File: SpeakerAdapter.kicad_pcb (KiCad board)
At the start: 2 copper layers, 14 x 12 mm, 2 parts, among them J1 Terminal Block, J2 JST-PH

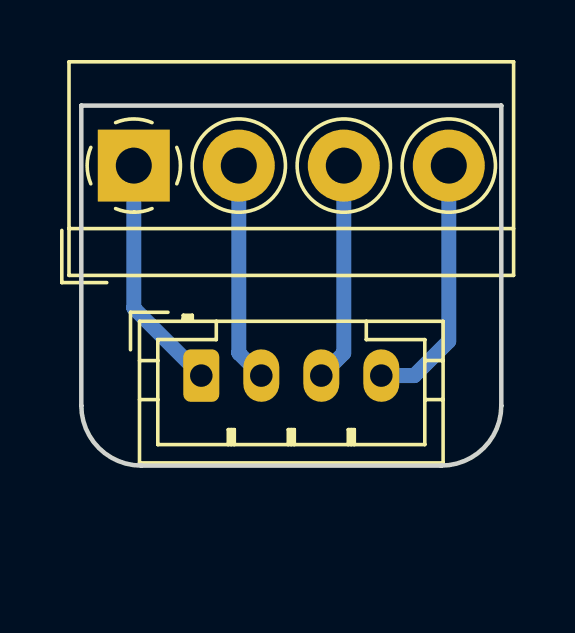
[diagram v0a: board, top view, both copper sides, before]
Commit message: Update PCB for right-angle JST-PH.
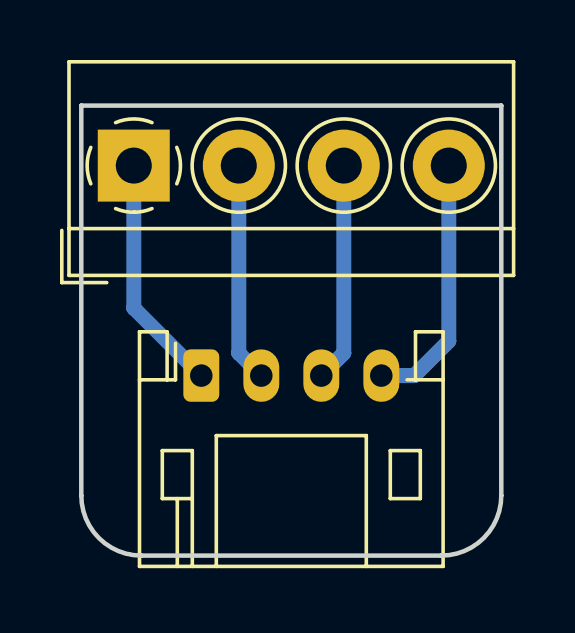
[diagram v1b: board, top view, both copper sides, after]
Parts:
- J2: footprint Connector_JST:JST_PH_B4B-PH-K_1x04_P2.00mm_Vertical -> Connector_JST:JST_PH_S4B-PH-K_1x04_P2.00mm_Horizontal
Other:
- board size 14 x 12 mm -> 14 x 15 mm
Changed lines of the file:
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@@
     )
   )
-  (module Connector_JST:JST_PH_B4B-PH-K_1x04_P2.00mm_Vertical (layer F.Cu)
+  (module Connector_JST:JST_PH_S4B-PH-K_1x04_P2.00mm_Horizontal (layer F.Cu)
     (at 157 67)
-    (descr "JST PH series connector, B4B-PH-K (http://www.jst-mfg.com/product/pdf/eng/ePH.pdf), generated with kicad-footprint-generator")
-    (tags "connector JST PH side entry")
-    (fp_text reference J2 (at 3 -2.9) (layer F.SilkS) hide
+    (descr "JST PH series connector, S4B-PH-K (http://www.jst-mfg.com/product/pdf/eng/ePH.pdf), generated with kicad-footprint-generator")
+    (tags "connector JST PH top entry")
+    (fp_text reference J2 (at 3 -2.55) (layer F.SilkS) hide
       (effects (font (size 1 1) (thickness 0.15)))
     )
-    (fp_text value JST-PH (at 3 4) (layer F.Fab)
+    (fp_text value JST-PH (at 3 7.45) (layer F.Fab)
       (effects (font (size 1 1) (thickness 0.15)))
     )
-    (fp_line (start -2.06 -1.81) (end -2.06 2.91) (layer F.SilkS) (width 0.12))
-    (fp_line (start -2.06 2.91) (end 8.06 2.91) (layer F.SilkS) (width 0.12))
-    (fp_line (start 8.06 2.91) (end 8.06 -1.81) (layer F.SilkS) (width 0.12))
-    (fp_line (start 8.06 -1.81) (end -2.06 -1.81) (layer F.SilkS) (width 0.12))
-    (fp_line (start -0.3 -1.81) (end -0.3 -2.01) (layer F.SilkS) (width 0.12))
-    (fp_line (start -0.3 -2.01) (end -0.6 -2.01) (layer F.SilkS) (width 0.12))
-    (fp_line (start -0.6 -2.01) (end -0.6 -1.81) (layer F.SilkS) (width 0.12))
-    (fp_line (start -0.3 -1.91) (end -0.6 -1.91) (layer F.SilkS) (width 0.12))
-    (fp_line (start 0.5 -1.81) (end 0.5 -1.2) (layer F.SilkS) (width 0.12))
-    (fp_line (start 0.5 -1.2) (end -1.45 -1.2) (layer F.SilkS) (width 0.12))
-    (fp_line (start -1.45 -1.2) (end -1.45 2.3) (layer F.SilkS) (width 0.12))
-    (fp_line (start -1.45 2.3) (end 7.45 2.3) (layer F.SilkS) (width 0.12))
-    (fp_line (start 7.45 2.3) (end 7.45 -1.2) (layer F.SilkS) (width 0.12))
-    (fp_line (start 7.45 -1.2) (end 5.5 -1.2) (layer F.SilkS) (width 0.12))
-    (fp_line (start 5.5 -1.2) (end 5.5 -1.81) (layer F.SilkS) (width 0.12))
-    (fp_line (start -2.06 -0.5) (end -1.45 -0.5) (layer F.SilkS) (width 0.12))
-    (fp_line (start -2.06 0.8) (end -1.45 0.8) (layer F.SilkS) (width 0.12))
-    (fp_line (start 8.06 -0.5) (end 7.45 -0.5) (layer F.SilkS) (width 0.12))
-    (fp_line (start 8.06 0.8) (end 7.45 0.8) (layer F.SilkS) (width 0.12))
-    (fp_line (start 0.9 2.3) (end 0.9 1.8) (layer F.SilkS) (width 0.12))
-    (fp_line (start 0.9 1.8) (end 1.1 1.8) (layer F.SilkS) (width 0.12))
-    (fp_line (start 1.1 1.8) (end 1.1 2.3) (layer F.SilkS) (width 0.12))
-    (fp_line (start 1 2.3) (end 1 1.8) (layer F.SilkS) (width 0.12))
-    (fp_line (start 2.9 2.3) (end 2.9 1.8) (layer F.SilkS) (width 0.12))
-    (fp_line (start 2.9 1.8) (end 3.1 1.8) (layer F.SilkS) (width 0.12))
-    (fp_line (start 3.1 1.8) (end 3.1 2.3) (layer F.SilkS) (width 0.12))
-    (fp_line (start 3 2.3) (end 3 1.8) (layer F.SilkS) (width 0.12))
-    (fp_line (start 4.9 2.3) (end 4.9 1.8) (layer F.SilkS) (width 0.12))
-    (fp_line (start 4.9 1.8) (end 5.1 1.8) (layer F.SilkS) (width 0.12))
-    (fp_line (start 5.1 1.8) (end 5.1 2.3) (layer F.SilkS) (width 0.12))
-    (fp_line (start 5 2.3) (end 5 1.8) (layer F.SilkS) (width 0.12))
-    (fp_line (start -1.11 -2.11) (end -2.36 -2.11) (layer F.SilkS) (width 0.12))
-    (fp_line (start -2.36 -2.11) (end -2.36 -0.86) (layer F.SilkS) (width 0.12))
-    (fp_line (start -1.11 -2.11) (end -2.36 -2.11) (layer F.Fab) (width 0.1))
-    (fp_line (start -2.36 -2.11) (end -2.36 -0.86) (layer F.Fab) (width 0.1))
-    (fp_line (start -1.95 -1.7) (end -1.95 2.8) (layer F.Fab) (width 0.1))
-    (fp_line (start -1.95 2.8) (end 7.95 2.8) (layer F.Fab) (width 0.1))
-    (fp_line (start 7.95 2.8) (end 7.95 -1.7) (layer F.Fab) (width 0.1))
-    (fp_line (start 7.95 -1.7) (end -1.95 -1.7) (layer F.Fab) (width 0.1))
-    (fp_line (start -2.45 -2.2) (end -2.45 3.3) (layer F.CrtYd) (width 0.05))
-    (fp_line (start -2.45 3.3) (end 8.45 3.3) (layer F.CrtYd) (width 0.05))
-    (fp_line (start 8.45 3.3) (end 8.45 -2.2) (layer F.CrtYd) (width 0.05))
-    (fp_line (start 8.45 -2.2) (end -2.45 -2.2) (layer F.CrtYd) (width 0.05))
-    (fp_text user %R (at 3 1.5) (layer F.Fab)
+    (fp_line (start -0.86 0.14) (end -1.14 0.14) (layer F.SilkS) (width 0.12))
+    (fp_line (start -1.14 0.14) (end -1.14 -1.46) (layer F.SilkS) (width 0.12))
+    (fp_line (start -1.14 -1.46) (end -2.06 -1.46) (layer F.SilkS) (width 0.12))
+    (fp_line (start -2.06 -1.46) (end -2.06 6.36) (layer F.SilkS) (width 0.12))
+    (fp_line (start -2.06 6.36) (end 8.06 6.36) (layer F.SilkS) (width 0.12))
+    (fp_line (start 8.06 6.36) (end 8.06 -1.46) (layer F.SilkS) (width 0.12))
+    (fp_line (start 8.06 -1.46) (end 7.14 -1.46) (layer F.SilkS) (width 0.12))
+    (fp_line (start 7.14 -1.46) (end 7.14 0.14) (layer F.SilkS) (width 0.12))
+    (fp_line (start 7.14 0.14) (end 6.86 0.14) (layer F.SilkS) (width 0.12))
+    (fp_line (start 0.5 6.36) (end 0.5 2) (layer F.SilkS) (width 0.12))
+    (fp_line (start 0.5 2) (end 5.5 2) (layer F.SilkS) (width 0.12))
+    (fp_line (start 5.5 2) (end 5.5 6.36) (layer F.SilkS) (width 0.12))
+    (fp_line (start -2.06 0.14) (end -1.14 0.14) (layer F.SilkS) (width 0.12))
+    (fp_line (start 8.06 0.14) (end 7.14 0.14) (layer F.SilkS) (width 0.12))
+    (fp_line (start -1.3 2.5) (end -1.3 4.1) (layer F.SilkS) (width 0.12))
+    (fp_line (start -1.3 4.1) (end -0.3 4.1) (layer F.SilkS) (width 0.12))
+    (fp_line (start -0.3 4.1) (end -0.3 2.5) (layer F.SilkS) (width 0.12))
+    (fp_line (start -0.3 2.5) (end -1.3 2.5) (layer F.SilkS) (width 0.12))
+    (fp_line (start 7.3 2.5) (end 7.3 4.1) (layer F.SilkS) (width 0.12))
+    (fp_line (start 7.3 4.1) (end 6.3 4.1) (layer F.SilkS) (width 0.12))
+    (fp_line (start 6.3 4.1) (end 6.3 2.5) (layer F.SilkS) (width 0.12))
+    (fp_line (start 6.3 2.5) (end 7.3 2.5) (layer F.SilkS) (width 0.12))
+    (fp_line (start -0.3 4.1) (end -0.3 6.36) (layer F.SilkS) (width 0.12))
+    (fp_line (start -0.8 4.1) (end -0.8 6.36) (layer F.SilkS) (width 0.12))
+    (fp_line (start -2.45 -1.85) (end -2.45 6.75) (layer F.CrtYd) (width 0.05))
+    (fp_line (start -2.45 6.75) (end 8.45 6.75) (layer F.CrtYd) (width 0.05))
+    (fp_line (start 8.45 6.75) (end 8.45 -1.85) (layer F.CrtYd) (width 0.05))
+    (fp_line (start 8.45 -1.85) (end -2.45 -1.85) (layer F.CrtYd) (width 0.05))
+    (fp_line (start -1.25 0.25) (end -1.25 -1.35) (layer F.Fab) (width 0.1))
+    (fp_line (start -1.25 -1.35) (end -1.95 -1.35) (layer F.Fab) (width 0.1))
+    (fp_line (start -1.95 -1.35) (end -1.95 6.25) (layer F.Fab) (width 0.1))
+    (fp_line (start -1.95 6.25) (end 7.95 6.25) (layer F.Fab) (width 0.1))
+    (fp_line (start 7.95 6.25) (end 7.95 -1.35) (layer F.Fab) (width 0.1))
+    (fp_line (start 7.95 -1.35) (end 7.25 -1.35) (layer F.Fab) (width 0.1))
+    (fp_line (start 7.25 -1.35) (end 7.25 0.25) (layer F.Fab) (width 0.1))
+    (fp_line (start 7.25 0.25) (end -1.25 0.25) (layer F.Fab) (width 0.1))
+    (fp_line (start -0.86 0.14) (end -0.86 -1.075) (layer F.SilkS) (width 0.12))
+    (fp_line (start 0 0.875) (end -0.5 1.375) (layer F.Fab) (width 0.1))
+    (fp_line (start -0.5 1.375) (end 0.5 1.375) (layer F.Fab) (width 0.1))
+    (fp_line (start 0.5 1.375) (end 0 0.875) (layer F.Fab) (width 0.1))
+    (fp_text user %R (at 3 2.5) (layer F.Fab)
       (effects (font (size 1 1) (thickness 0.15)))
     )
@@
     (pad 4 thru_hole oval (at 6 0) (size 1.2 1.75) (drill 0.75) (layers *.Cu *.Mask)
       (net 4 "Net-(J1-Pad4)"))
-    (model ${KISYS3DMOD}/Connector_JST.3dshapes/JST_PH_B4B-PH-K_1x04_P2.00mm_Vertical.wrl
+    (model ${KISYS3DMOD}/Connector_JST.3dshapes/JST_PH_S4B-PH-K_1x04_P2.00mm_Horizontal.wrl
       (at (xyz 0 0 0))
       (scale (xyz 1 1 1))
@@
     )
   )
-  (gr_arc (start 155 68) (end 153 68) (angle -90) (layer Edge.Cuts) (width 0.15))
-  (gr_arc (start 165 68) (end 165 70) (angle -90) (layer Edge.Cuts) (width 0.15))
+  (gr_arc (start 155 71) (end 153 71) (angle -90) (layer Edge.Cuts) (width 0.15))
+  (gr_arc (start 165 71) (end 165 73) (angle -90) (layer Edge.Cuts) (width 0.15))
   (gr_text "Speaker Adapter\nPEP 2019-08-24" (at 160 64) (layer B.SilkS)
     (effects (font (size 1 1) (thickness 0.2)) (justify mirror))
   )
-  (gr_line (start 153 68) (end 153 58) (layer Edge.Cuts) (width 0.15))
-  (gr_line (start 165 70) (end 155 70) (layer Edge.Cuts) (width 0.15))
-  (gr_line (start 167 58) (end 167 68) (layer Edge.Cuts) (width 0.15))
+  (gr_line (start 153 71) (end 153 58) (layer Edge.Cuts) (width 0.15))
+  (gr_line (start 165 73) (end 155 73) (layer Edge.Cuts) (width 0.15))
+  (gr_line (start 167 58) (end 167 71) (layer Edge.Cuts) (width 0.15))
   (gr_line (start 153 58) (end 167 58) (layer Edge.Cuts) (width 0.15))
   (segment (start 154.75 64.75) (end 157 67) (width 0.5) (layer B.Cu) (net 1))

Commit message: Extend by 0.5mm.
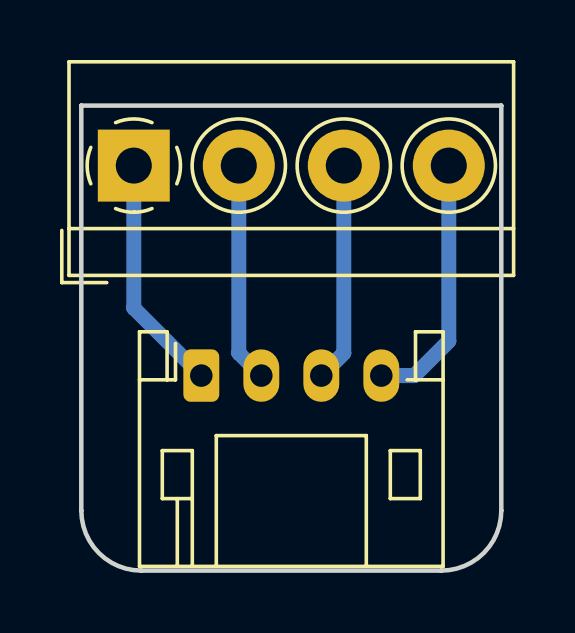
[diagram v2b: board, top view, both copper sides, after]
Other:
- board size 14 x 15 mm -> 14 x 15.5 mm
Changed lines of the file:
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@@
     )
   )
-  (gr_arc (start 155 71) (end 153 71) (angle -90) (layer Edge.Cuts) (width 0.15))
-  (gr_arc (start 165 71) (end 165 73) (angle -90) (layer Edge.Cuts) (width 0.15))
+  (gr_arc (start 155 71.5) (end 153 71.5) (angle -90) (layer Edge.Cuts) (width 0.15))
+  (gr_arc (start 165 71.5) (end 165 73.5) (angle -90) (layer Edge.Cuts) (width 0.15))
   (gr_text "Speaker Adapter\nPEP 2019-08-24" (at 160 64) (layer B.SilkS)
     (effects (font (size 1 1) (thickness 0.2)) (justify mirror))
   )
-  (gr_line (start 153 71) (end 153 58) (layer Edge.Cuts) (width 0.15))
-  (gr_line (start 165 73) (end 155 73) (layer Edge.Cuts) (width 0.15))
-  (gr_line (start 167 58) (end 167 71) (layer Edge.Cuts) (width 0.15))
+  (gr_line (start 153 71.5) (end 153 58) (layer Edge.Cuts) (width 0.15))
+  (gr_line (start 165 73.5) (end 155 73.5) (layer Edge.Cuts) (width 0.15))
+  (gr_line (start 167 58) (end 167 71.5) (layer Edge.Cuts) (width 0.15))
   (gr_line (start 153 58) (end 167 58) (layer Edge.Cuts) (width 0.15))
   (segment (start 154.75 64.75) (end 157 67) (width 0.5) (layer B.Cu) (net 1))

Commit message: Updated PCB with new terminal block footprint.
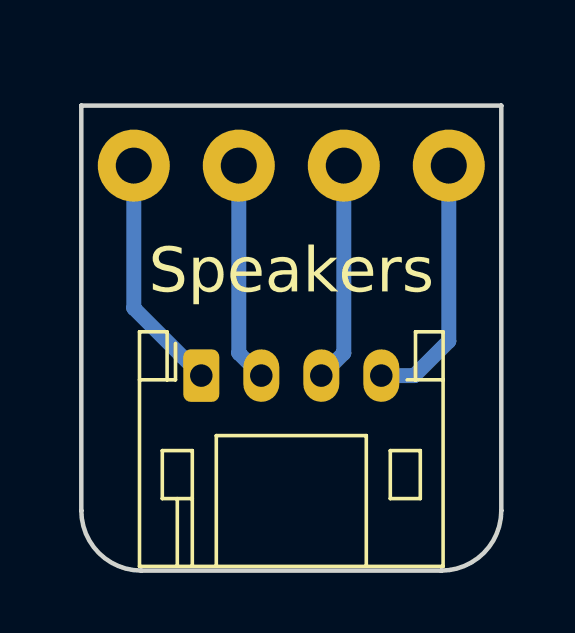
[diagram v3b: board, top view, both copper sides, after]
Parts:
- J1: footprint TerminalBlock_4Ucon:TerminalBlock_4Ucon_1x04_P3.50mm_Horizontal -> local:TerminalBlock_4Ucon_1x04_P3.50mm_Horizontal
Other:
- board text added: "Speakers"
